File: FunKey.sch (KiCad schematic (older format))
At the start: 216 parts, among them J1 MH3-1-0.05, J2 U02-BFD3111B0-009, J3 DF37NB-24DS-0.4V, J4 TF-110, J5 SM02B-SRSS-TB, Q1 IRLML2244TRPBF, U1 PCAL6416AHF,128, U2 PAM8301AAF, U3 V3S, U4 SY8088AAC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

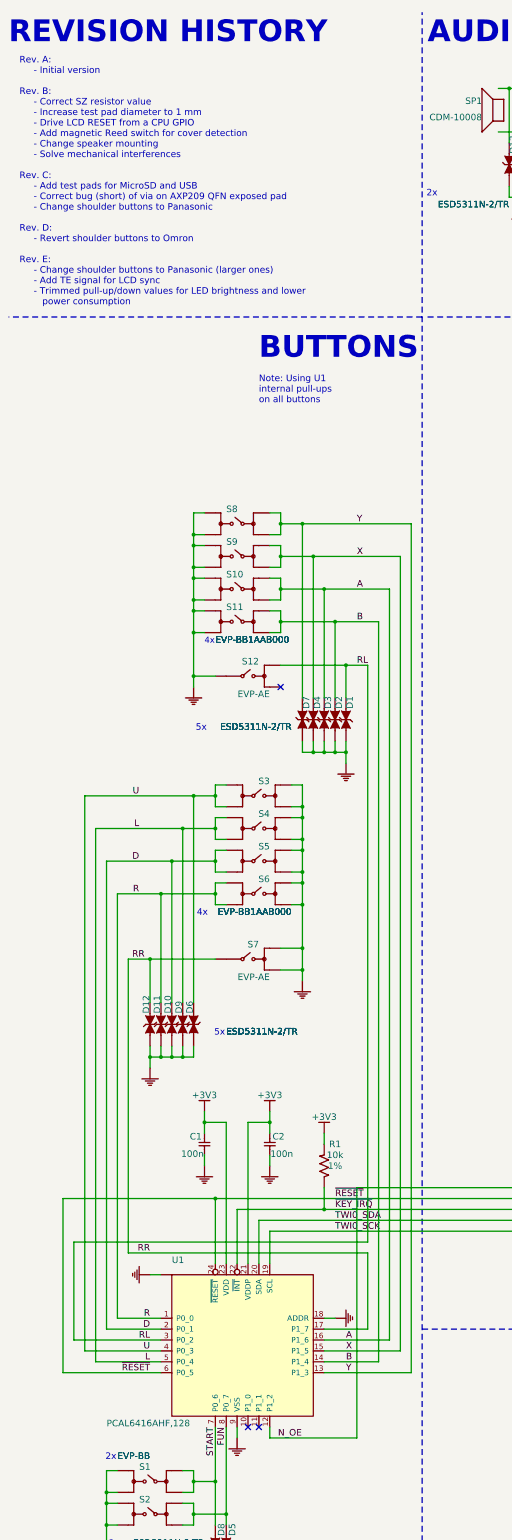
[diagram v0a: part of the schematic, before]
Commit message: Revision F with 0.3mm increased length speaker tabs and added drills in the side button corners to make cutout square
Signed-off-by: Michel-FK <michel.stempin@funkey-project.com>
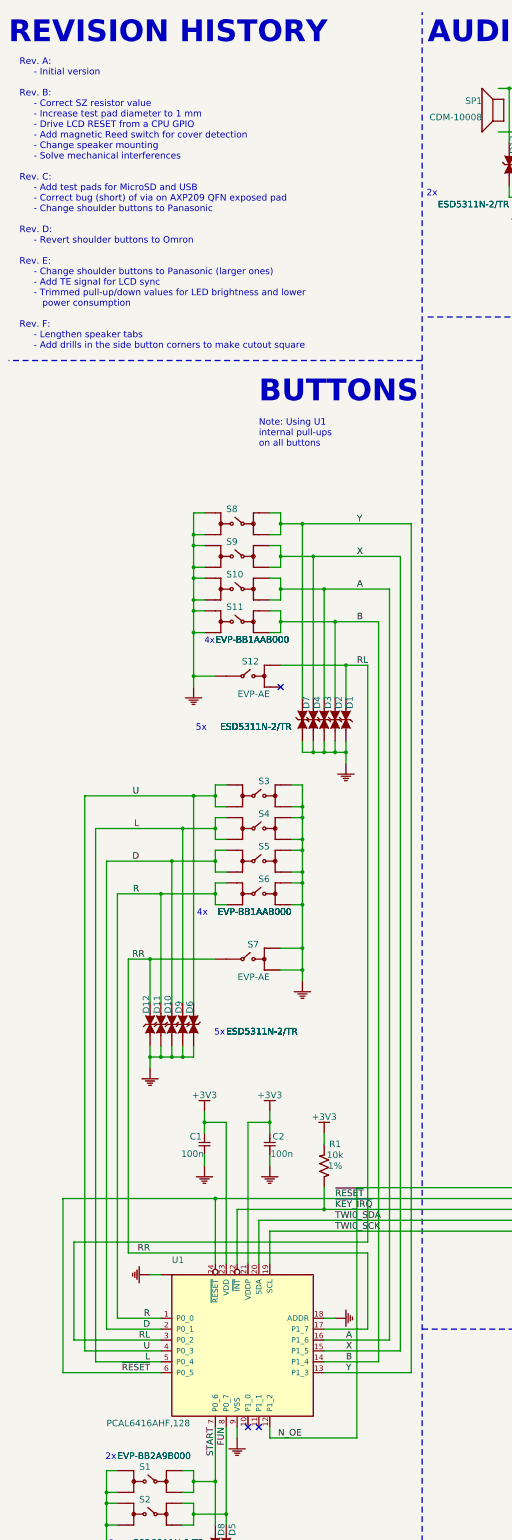
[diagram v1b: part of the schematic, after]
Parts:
- S1, S2: value EVP-BB -> EVP-BB2A9B000
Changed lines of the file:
@@
 Sheet 1 1
 Title "FunKey"
-Date "2020/11/26"
-Rev "E"
-Comp "© 2017-2020 Michel Stempin, All rights reserved."
+Date "2021/03/22"
+Rev "f"
+Comp "© 2017-2021 Michel Stempin, All rights reserved."
 Comment1 ""
 Comment2 ""
@@
 P 1800 14000
 F 0 "S1" H 1700 14100 60  0000 L BNN
-F 1 "EVP-BB" H 1500 14200 60  0000 L BNN
+F 1 "EVP-BB2A9B000" H 1500 14200 60  0000 L BNN
 F 2 "FunKey:EVP-BB" H 1800 14000 50  0001 C CNN
 F 3 "" H 1800 14000 50  0001 C CNN
@@
 P 1800 14300
 F 0 "S2" H 1700 14400 60  0000 L BNN
-F 1 "EVP-BB" H 1500 14800 60  0000 L BNN
+F 1 "EVP-BB2A9B000" H 1500 14800 60  0000 L BNN
 F 2 "FunKey:EVP-BB" H 1800 14300 50  0001 C CNN
 F 3 "" H 1800 14300 50  0001 C CNN
@@
 Text Notes 4340 2200 0    60   ~ 0
 2x
-Text Notes 2800 3700 0    200  ~ 40
+Text Notes 2800 4100 0    200  ~ 40
 BUTTONS
 Text Notes 1420 14610 0    60   ~ 0
@@
 Text Notes 2390 9910 0    59   ~ 0
 5x
-Text Notes 2800 4100 0    60   ~ 0
+Text Notes 2800 4500 0    60   ~ 0
 Note: Using U1\ninternal pull-ups\non all buttons
 Text Notes 2300 6310 0    56   ~ 0
@@
 Wire Notes Line
 	10100 12650 10100 16050
-Text Notes 600  3200 0    60   ~ 0
-Rev. A:\n     - Initial version\n\nRev. B:\n     - Correct SZ resistor value\n     - Increase test pad diameter to 1 mm\n     - Drive LCD RESET from a CPU GPIO\n     - Add magnetic Reed switch for cover detection\n     - Change speaker mounting\n     - Solve mechanical interferences\n\nRev. C:\n     - Add test pads for MicroSD and USB\n     - Correct bug (short) of via on AXP209 QFN exposed pad\n     - Change shoulder buttons to Panasonic\n\nRev. D:\n     - Revert shoulder buttons to Omron\n\nRev. E:\n     - Change shoulder buttons to Panasonic (larger ones)\n     - Add TE signal for LCD sync\n     - Trimmed pull-up/down values for LED brightness and lower\n        power consumption\n
 Wire Notes Line
-	4300 3300 500  3300
+	4300 3700 500  3700
 Text Notes 500  800  0    200  ~ 40
 REVISION HISTORY
@@
 Wire Wire Line
 	11900 10800 11900 11900
+Text Notes 600  3600 0    60   ~ 0
+Rev. A:\n     - Initial version\n\nRev. B:\n     - Correct SZ resistor value\n     - Increase test pad diameter to 1 mm\n     - Drive LCD RESET from a CPU GPIO\n     - Add magnetic Reed switch for cover detection\n     - Change speaker mounting\n     - Solve mechanical interferences\n\nRev. C:\n     - Add test pads for MicroSD and USB\n     - Correct bug (short) of via on AXP209 QFN exposed pad\n     - Change shoulder buttons to Panasonic\n\nRev. D:\n     - Revert shoulder buttons to Omron\n\nRev. E:\n     - Change shoulder buttons to Panasonic (larger ones)\n     - Add TE signal for LCD sync\n     - Trimmed pull-up/down values for LED brightness and lower\n        power consumption\n\nRev. F:\n     - Lengthen speaker tabs\n     - Add drills in the side button corners to make cutout square
 $EndSCHEMATC
